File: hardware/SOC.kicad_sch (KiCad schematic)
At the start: 67 parts, among them J3 TF01-A, P1 HRO-TYPE-C-31-M-12, P2 WF24HTLAJDNN0#, Q1 Q_NMOS_DSG, SW2 TS-1157-X-F, SW3 TS-1157-X-F, SW4 TS-1157-X-F, SW5 TS-1157-X-F, SW6 TS-1157-X-F, SW7 TS-1010-C-A, SW8 TS-1010-C-A, U12 W25Q128JVSIQ, U4 F1C200S, U8 USBLC6-2SC6, Y1 Crystal_GND24

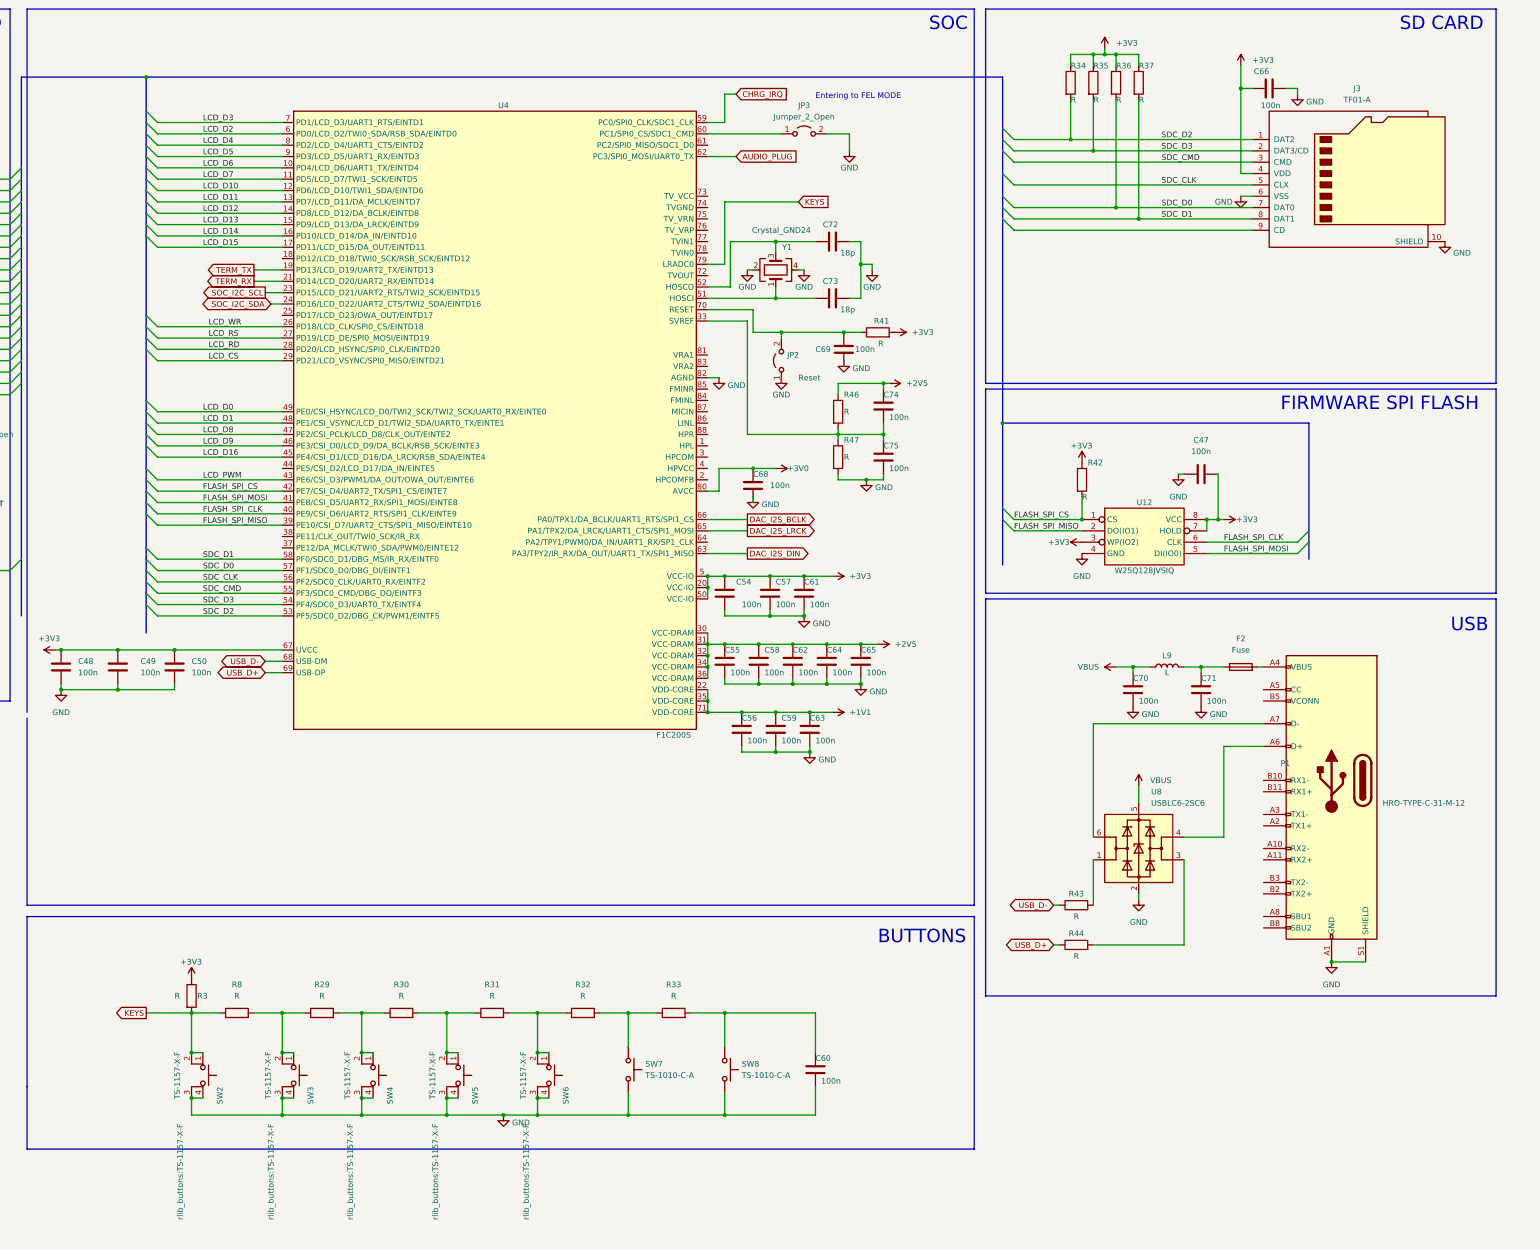
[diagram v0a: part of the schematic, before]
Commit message: added hierarchy labels
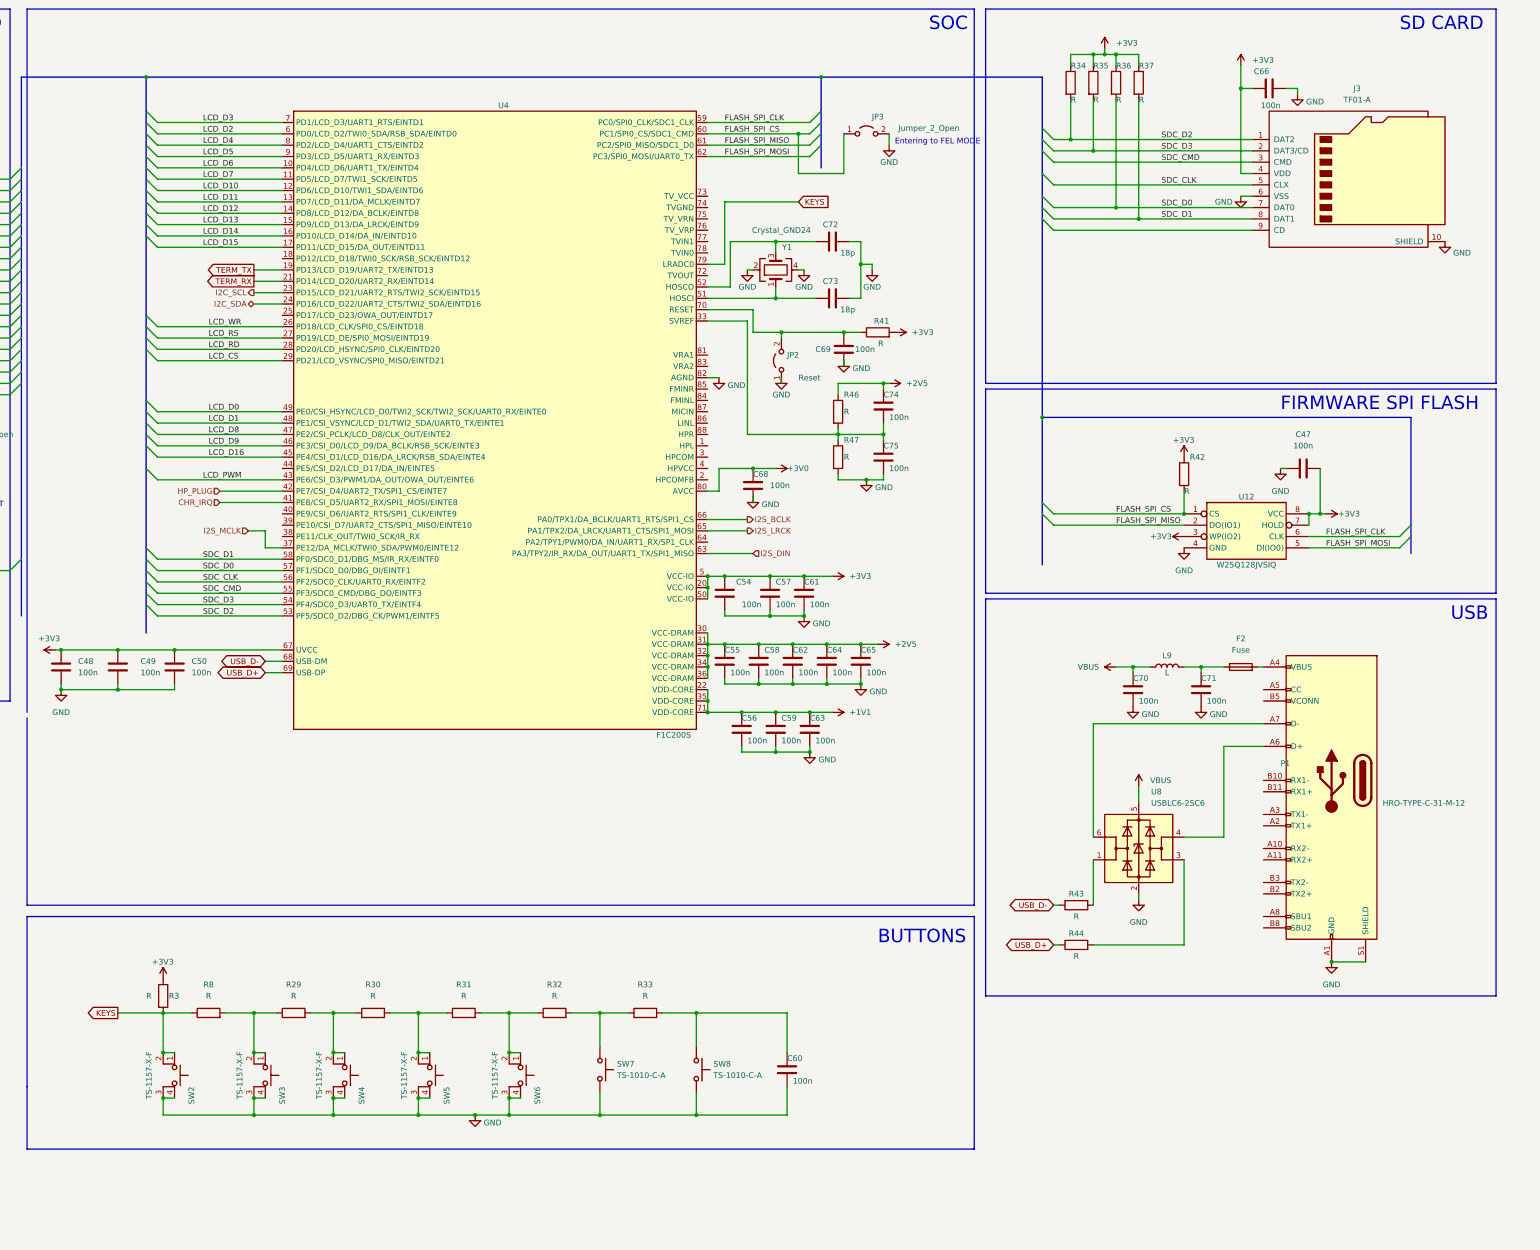
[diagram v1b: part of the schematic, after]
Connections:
- net AUDIO_PLUG is gone; now on net FLASH_SPI_MOSI: U4.62 (PC3/SPI0_MOSI/UART0_TX)
- net CHRG_IRQ is gone; now on net FLASH_SPI_CLK: U4.59 (PC0/SPI0_CLK/SDC1_CLK)
- net FLASH_SPI_CLK: no longer U4.40 (PE9/CSI_D6/UART2_RTS/SPI1_CLK/EINTE9)
- net FLASH_SPI_CS: now also JP3.1 (A), U4.60 (PC1/SPI0_CS/SDC1_CMD); no longer U4.42 (PE7/CSI_D4/UART2_TX/SPI1_CS/EINTE7)
- net FLASH_SPI_MISO: now also U4.61 (PC2/SPI0_MISO/SDC1_D0); no longer U4.39 (PE10/CSI_D7/UART2_CTS/SPI1_MISO/EINTE10)
- net FLASH_SPI_MOSI: no longer U4.41 (PE8/CSI_D5/UART2_RX/SPI1_MOSI/EINTE8)
- net I2S_MCLK: now reaches U4.37 (PE12/DA_MCLK/TWI0_SDA/PWM0/EINTE12)
- net DAC_I2S_BCLK renamed I2S_BCLK
- net DAC_I2S_DIN renamed I2S_DIN
- net DAC_I2S_LRCK renamed I2S_LRCK
- net SOC_I2C_SCL renamed I2C_SCL
- net SOC_I2C_SDA renamed I2C_SDA
- new net CHR_IRQ: U4.41 (PE8/CSI_D5/UART2_RX/SPI1_MOSI/EINTE8)
- new net HP_PLUG: U4.42 (PE7/CSI_D4/UART2_TX/SPI1_CS/EINTE7)
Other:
- moved on the sheet: C47, C60, JP3, R29, R3, R30, R31, R32, R33, R42, R8, SW2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

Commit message: added esd protection
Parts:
- added D? (x7): PESD3V3L1BA, rlib_passive:D_SOD-323F, symbol rlib_passive:PESD3V3L1BA
- added TP? (x2): TestPoint, symbol Connector:TestPoint
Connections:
- net GND: now also D?.1 (A1), D?.1 (A1), D?.1 (A1), D?.1 (A1), D?.1 (A1), D?.1 (A1), D?.1 (A1)
- net SDC_CLK: now also D?.2 (A2)
- net SDC_CMD: now also D?.2 (A2)
- net SDC_D0: now also D?.2 (A2)
- net SDC_D1: now also D?.2 (A2)
- net SDC_D2: now also D?.2 (A2)
- net SDC_D3: now also D?.2 (A2)
- net TERM_RX: now also TP?.1
- net TERM_TX: now also TP?.1
- net at C60.1, R33.2, SW8.1: now also D?.2 (A2)
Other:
- moved on the sheet: C66, C70, C71, F2, J3, L9, P1, R43, R44, U8

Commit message: replaced dc-dc ics
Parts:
- removed R42: R, rlib_passive:R_0603_1608Metric, symbol rlib_passive:R
- removed U12: W25Q128JVSIQ, rlib_ic:SOIC-8_5.23x5.23mm_P1.27mm, symbol rlib_ic:W25Q128JVSIQ
- added R48: R, rlib_passive:R_0603_1608Metric, symbol rlib_passive:R
- added TP? (x6): TestPoint, symbol Connector:TestPoint
- added U12: MX25L25635F, rlib_ic:SON127P600X800X80-9N, symbol rlib_ic:MX25L25635F
- gave numbers to parts that had none: 9
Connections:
- net +3V3: now also R48.1, U12.8 (VCC)
- net FLASH_SPI_CLK: now also U12.6 (SCLK)
- net FLASH_SPI_CS: now also U12.1 (~{CS})
- net FLASH_SPI_MISO: now also U12.2 (SO/SIO1)
- net FLASH_SPI_MOSI: now also U12.5 (SI/SIO0)
- net GND: now also U12.4 (GND)
- net I2C_SCL: now also TP?.1
- net I2C_SDA: now also TP?.1
- net I2S_BCLK: now also TP?.1
- net I2S_DIN: now also TP?.1
- net I2S_LRCK: now also TP?.1
- net I2S_MCLK: now also TP?.1
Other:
- moved on the sheet: C47, C60, C68, C74, C75, D4, JP2, R41, R46, R47, TP10, TP9

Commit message: some changes
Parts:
- removed R48: R, rlib_passive:R_0603_1608Metric, symbol rlib_passive:R
- R29, R3, R30, R31, R32, R33, R8: value R -> 10k
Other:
- note added: "DOWN"
- note added: "ENTER"
- note added: "LEFT"
- note added: "RIGHT"
- note added: "UP"
- note added: "VOL_DOWN"
- note added: "VOL_UP"
- moved on the sheet: C60, D4

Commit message: sfsf
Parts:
- SW2, SW3, SW4, SW5, SW6: value TS-1157-X-F -> K2-1156SP-F5SW-05; footprint rlib_buttons:TS-1157-X-F -> rlib_buttons:K2-1156SP-F5SW-05; symbol rlib_buttons:TS-1157-X-F -> rlib_buttons:K2-1156SP-F5SW-05
- SW7, SW8: footprint rlib_buttons:TS-1010-X-X -> rlib_buttons:GT-TC054A-H035-L1; symbol rlib_buttons:TS-1010-C-A -> rlib_buttons:GT-TC054A-H035-L1
- gave numbers to parts that had none: 6
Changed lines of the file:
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@@
     (pin "1")
   )
-  (symbol (lib_id "rlib_buttons:TS-1157-X-F") (at 100.33 262.89 270) (unit 1)
+  (symbol (lib_id "rlib_buttons:K2-1156SP-F5SW-05") (at 100.33 262.89 270) (unit 1)
     (in_bom yes) (on_board yes)
     (property "Reference" "SW2" (id 0) (at 106.68 265.43 0)
       (effects (font (size 1.27 1.27)) (justify left))
     )
-    (property "Value" "TS-1157-X-F" (id 1) (at 97.155 262.89 0))
-    (property "Footprint" "rlib_buttons:TS-1157-X-F" (id 2) (at 97.79 284.48 0)
+    (property "Value" "K2-1156SP-F5SW-05" (id 1) (at 97.155 262.89 0))
+    (property "Footprint" "rlib_buttons:K2-1156SP-F5SW-05" (id 2) (at 97.79 284.48 0)
       (effects (font (size 1.27 1.27)) hide)
     )
@@
     (pin "2")
   )
-  (symbol (lib_id "rlib_buttons:TS-1010-C-A") (at 219.71 261.62 270) (unit 1)
+  (symbol (lib_id "rlib_buttons:GT-TC054A-H035-L1") (at 219.71 261.62 270) (unit 1)
     (in_bom yes) (on_board yes)
     (property "Reference" "SW8" (id 0) (at 223.52 260.3499 90)
@@
       (effects (font (size 1.27 1.27)) (justify left))
     )
-    (property "Footprint" "rlib_buttons:TS-1010-X-X" (id 2) (at 214.63 260.35 0)
+    (property "Footprint" "rlib_buttons:GT-TC054A-H035-L1" (id 2) (at 214.63 260.35 0)
       (effects (font (size 1.27 1.27)) hide)
     )
@@
   (symbol (lib_id "Connector:TestPoint") (at 252.73 135.89 0) (unit 1)
     (in_bom yes) (on_board yes)
-    (property "Reference" "TP?" (id 0) (at 251.46 129.54 0)
+    (property "Reference" "TP16" (id 0) (at 251.46 129.54 0)
       (effects (font (size 1.27 1.27)) (justify left))
     )
@@
     (pin "2")
   )
-  (symbol (lib_id "rlib_buttons:TS-1157-X-F") (at 138.43 262.89 270) (unit 1)
+  (symbol (lib_id "rlib_buttons:K2-1156SP-F5SW-05") (at 138.43 262.89 270) (unit 1)
     (in_bom yes) (on_board yes) (fields_autoplaced)
     (property "Reference" "SW4" (id 0) (at 144.78 265.43 0)
       (effects (font (size 1.27 1.27)) (justify left))
     )
-    (property "Value" "TS-1157-X-F" (id 1) (at 135.255 262.89 0))
-    (property "Footprint" "rlib_buttons:TS-1157-X-F" (id 2) (at 135.89 284.48 0)
+    (property "Value" "K2-1156SP-F5SW-05" (id 1) (at 135.255 262.89 0))
+    (property "Footprint" "rlib_buttons:K2-1156SP-F5SW-05" (id 2) (at 135.89 284.48 0)
       (effects (font (size 1.27 1.27)) hide)
     )
@@
     (pin "2")
   )
-  (symbol (lib_id "rlib_buttons:TS-1157-X-F") (at 177.8 262.89 270) (unit 1)
+  (symbol (lib_id "rlib_buttons:K2-1156SP-F5SW-05") (at 177.8 262.89 270) (unit 1)
     (in_bom yes) (on_board yes) (fields_autoplaced)
     (property "Reference" "SW6" (id 0) (at 184.15 265.43 0)
       (effects (font (size 1.27 1.27)) (justify left))
     )
-    (property "Value" "TS-1157-X-F" (id 1) (at 174.625 262.89 0))
-    (property "Footprint" "rlib_buttons:TS-1157-X-F" (id 2) (at 175.26 284.48 0)
+    (property "Value" "K2-1156SP-F5SW-05" (id 1) (at 174.625 262.89 0))
+    (property "Footprint" "rlib_buttons:K2-1156SP-F5SW-05" (id 2) (at 175.26 284.48 0)
       (effects (font (size 1.27 1.27)) hide)
     )
@@
   (symbol (lib_id "Connector:TestPoint") (at 111.76 86.36 0) (unit 1)
     (in_bom yes) (on_board yes)
-    (property "Reference" "TP?" (id 0) (at 110.49 80.01 0)
+    (property "Reference" "TP12" (id 0) (at 110.49 80.01 0)
       (effects (font (size 1.27 1.27)) (justify left))
     )
@@
     (pin "2")
   )
-  (symbol (lib_id "rlib_buttons:TS-1157-X-F") (at 120.65 262.89 270) (unit 1)
+  (symbol (lib_id "rlib_buttons:K2-1156SP-F5SW-05") (at 120.65 262.89 270) (unit 1)
     (in_bom yes) (on_board yes) (fields_autoplaced)
     (property "Reference" "SW3" (id 0) (at 127 265.43 0)
       (effects (font (size 1.27 1.27)) (justify left))
     )
-    (property "Value" "TS-1157-X-F" (id 1) (at 117.475 262.89 0))
-    (property "Footprint" "rlib_buttons:TS-1157-X-F" (id 2) (at 118.11 284.48 0)
+    (property "Value" "K2-1156SP-F5SW-05" (id 1) (at 117.475 262.89 0))
+    (property "Footprint" "rlib_buttons:K2-1156SP-F5SW-05" (id 2) (at 118.11 284.48 0)
       (effects (font (size 1.27 1.27)) hide)
     )
@@
   (symbol (lib_id "Connector:TestPoint") (at 247.65 135.89 0) (unit 1)
     (in_bom yes) (on_board yes)
-    (property "Reference" "TP?" (id 0) (at 246.38 129.54 0)
+    (property "Reference" "TP15" (id 0) (at 246.38 129.54 0)
       (effects (font (size 1.27 1.27)) (justify left))
     )
@@
   (symbol (lib_id "Connector:TestPoint") (at 119.38 142.24 0) (unit 1)
     (in_bom yes) (on_board yes)
-    (property "Reference" "TP?" (id 0) (at 118.11 135.89 0)
+    (property "Reference" "TP13" (id 0) (at 118.11 135.89 0)
       (effects (font (size 1.27 1.27)) (justify left))
     )
@@
     (pin "1")
   )
-  (symbol (lib_id "rlib_buttons:TS-1157-X-F") (at 157.48 262.89 270) (unit 1)
+  (symbol (lib_id "rlib_buttons:K2-1156SP-F5SW-05") (at 157.48 262.89 270) (unit 1)
     (in_bom yes) (on_board yes) (fields_autoplaced)
     (property "Reference" "SW5" (id 0) (at 163.83 265.43 0)
       (effects (font (size 1.27 1.27)) (justify left))
     )
-    (property "Value" "TS-1157-X-F" (id 1) (at 154.305 262.89 0))
-    (property "Footprint" "rlib_buttons:TS-1157-X-F" (id 2) (at 154.94 284.48 0)
+    (property "Value" "K2-1156SP-F5SW-05" (id 1) (at 154.305 262.89 0))
+    (property "Footprint" "rlib_buttons:K2-1156SP-F5SW-05" (id 2) (at 154.94 284.48 0)
       (effects (font (size 1.27 1.27)) hide)
     )
@@
   (symbol (lib_id "Connector:TestPoint") (at 243.84 135.89 0) (unit 1)
     (in_bom yes) (on_board yes)
-    (property "Reference" "TP?" (id 0) (at 242.57 129.54 0)
+    (property "Reference" "TP14" (id 0) (at 242.57 129.54 0)
       (effects (font (size 1.27 1.27)) (justify left))
     )
@@
     (pin "1")
   )
-  (symbol (lib_id "rlib_buttons:TS-1010-C-A") (at 198.12 261.62 270) (unit 1)
+  (symbol (lib_id "rlib_buttons:GT-TC054A-H035-L1") (at 198.12 261.62 270) (unit 1)
     (in_bom yes) (on_board yes)
     (property "Reference" "SW7" (id 0) (at 201.93 260.3499 90)
@@
       (effects (font (size 1.27 1.27)) (justify left))
     )
-    (property "Footprint" "rlib_buttons:TS-1010-X-X" (id 2) (at 193.04 260.35 0)
+    (property "Footprint" "rlib_buttons:GT-TC054A-H035-L1" (id 2) (at 193.04 260.35 0)
       (effects (font (size 1.27 1.27)) hide)
     )
@@
   (symbol (lib_id "Connector:TestPoint") (at 107.95 86.36 0) (unit 1)
     (in_bom yes) (on_board yes)
-    (property "Reference" "TP?" (id 0) (at 106.68 80.01 0)
-      (effects (font (size 1.27 1.27)) (justify left))
-    )
+    (property "Reference" "TP11" (id 0) (at 106.68 80.01 0)
+      (effects (font (size 1.27 1.27)) (justify left))
+    )

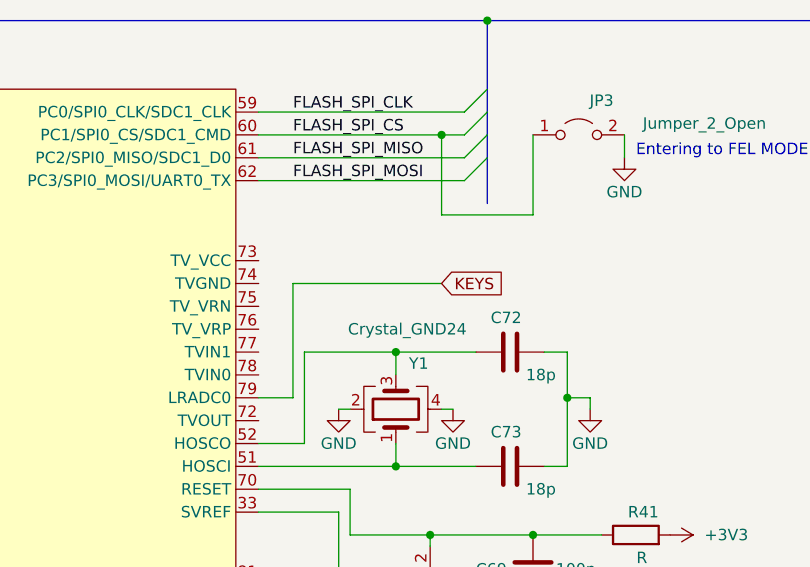
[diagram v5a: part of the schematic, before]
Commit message: added new power list
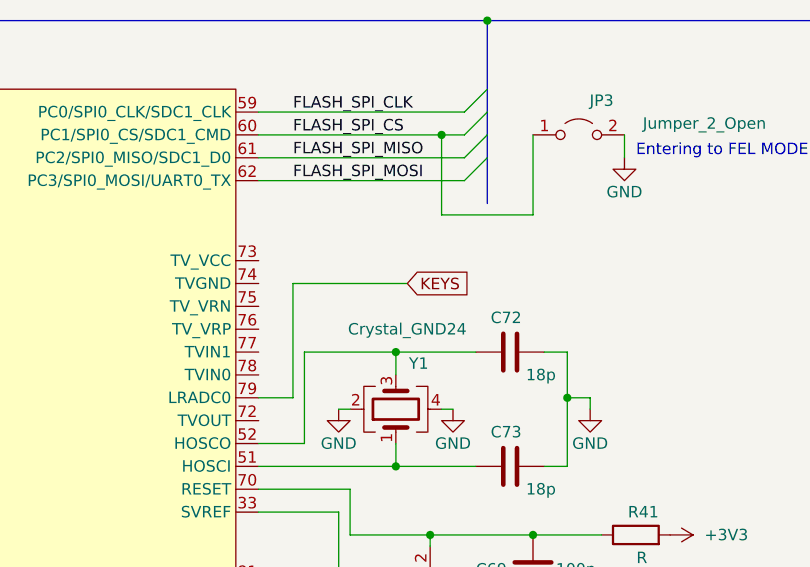
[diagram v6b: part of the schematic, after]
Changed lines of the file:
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@@
     (stroke (width 0) (type default) (color 0 0 0 0))
   )
-  (wire (pts (xy 242.57 68.58) (xy 226.06 68.58))
+  (wire (pts (xy 238.76 68.58) (xy 226.06 68.58))
     (stroke (width 0) (type default) (color 0 0 0 0))
   )
@@
     )
   )
-  (global_label "KEYS" (shape input) (at 242.57 68.58 0) (fields_autoplaced)
+  (global_label "KEYS" (shape input) (at 238.76 68.58 0) (fields_autoplaced)
     (effects (font (size 1.27 1.27)) (justify left))
-    (property "Intersheet References" "${INTERSHEET_REFS}" (id 0) (at 249.7002 68.5006 0)
+    (property "Intersheet References" "${INTERSHEET_REFS}" (id 0) (at 245.8902 68.5006 0)
       (effects (font (size 1.27 1.27)) (justify left) hide)
     )
